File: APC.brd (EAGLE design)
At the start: 24.9 x 56.8 mm, 12 parts, among them IC1 NE556D, J1 POWER_JACKPTH_SMD_COMBO, J3 AUDIO_JACK_3.5MM_PTH, P1 1M, P2 1M, P3 100k

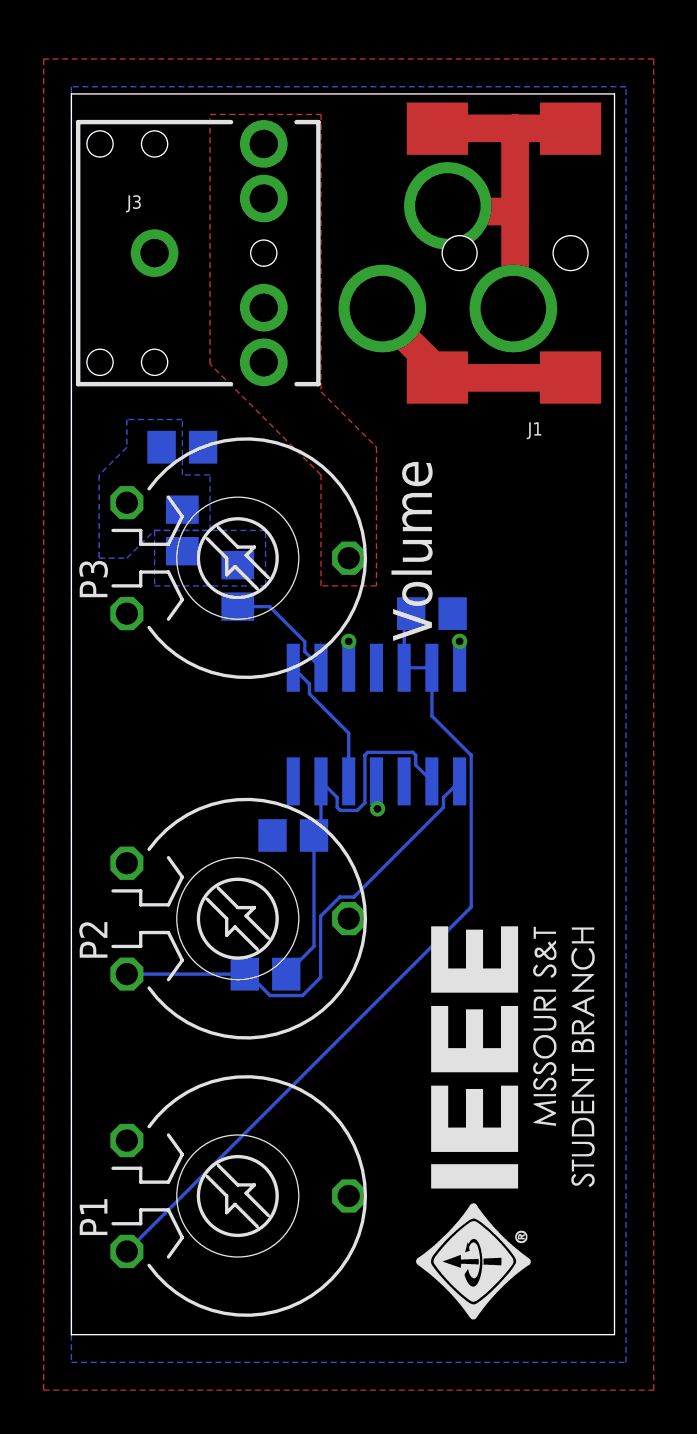
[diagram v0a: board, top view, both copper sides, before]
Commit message: V2
Updated schematic to use all digikey parts. Added solderable pads for power
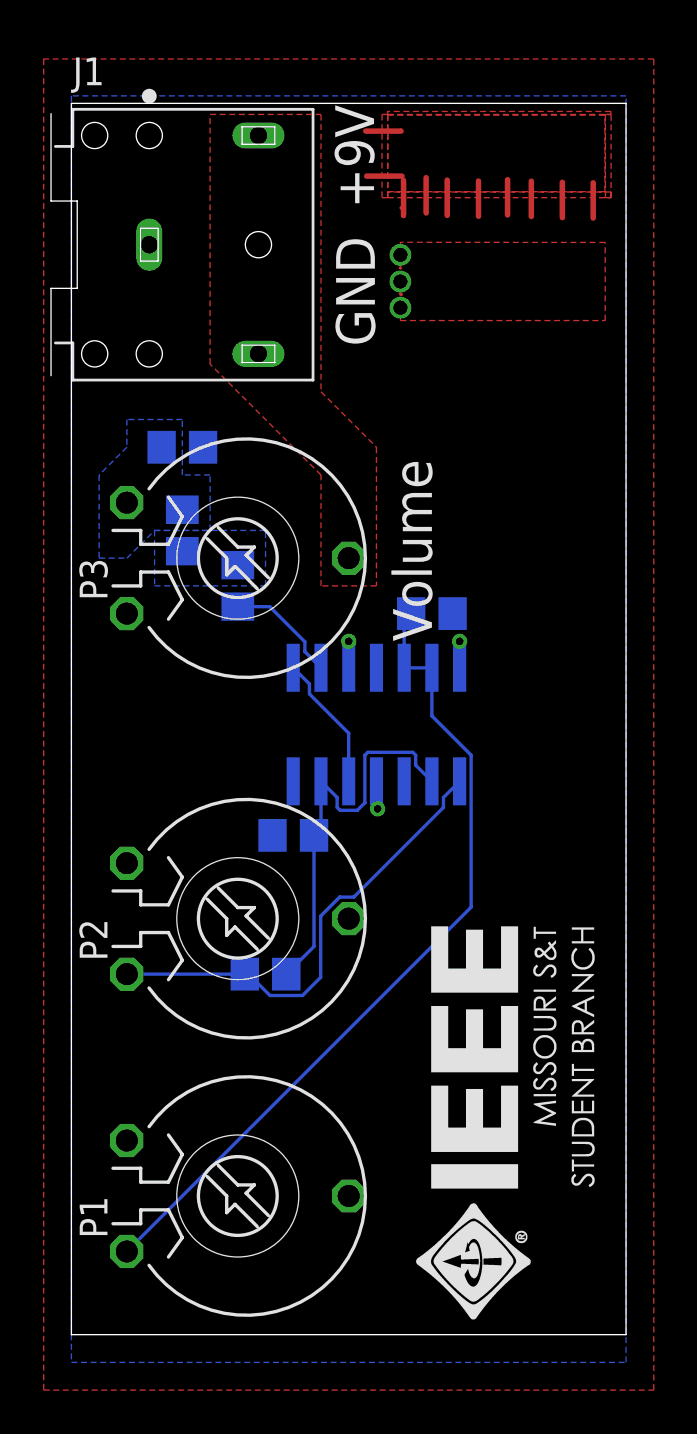
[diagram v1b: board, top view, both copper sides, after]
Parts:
- removed J3: AUDIO_JACK_3.5MM_PTH, SparkFun-Connectors:AUDIO-JACK
- J1: value POWER_JACKPTH_SMD_COMBO -> SJ1-3523N; device SparkFun-Connectors:POWER_JACK_COMBO -> SJ1-3523N:CUI_SJ1-3523N
- moved J1 19.3 mm to (3.57, 93.1), turned to 0 degrees
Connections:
- net +9V: no longer J1.POWER
- net GND: now also J1.1; no longer J1.GND, J1.GND@1, J3.SLEEVE
- net N$9: now also J1.2, J1.3; no longer J3.RING, J3.TIP
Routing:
- net +9V: track 3.70 -> 20.0 mm
- net N$9: track 0.63 -> 0.00 mm
- net GND: track 0.00 -> 0.06 mm, vias 0 -> 3
- added copper zone on layer 1, net GND
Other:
- board size 24.9 x 56.8 mm -> 25.4 x 56.4 mm
- board text added: "+9V"
- board text added: "GND"

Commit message: JLC Gerber created
Ready for ordering
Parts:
- renumbered R4 to R2, R6 to R3
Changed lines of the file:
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@@
 <attribute name="SPICEPREFIX" value="C" x="7.62" y="77.47" size="1.778" layer="28" rot="MR90" display="off"/>
 </element>
-<element name="R4" library="rcl" library_urn="urn:adsk.eagle:library:334" package="R0805" package3d_urn="urn:adsk.eagle:package:23553/2" value="10k" x="5.08" y="80.01" smashed="yes" rot="MR90">
+<element name="R2" library="rcl" library_urn="urn:adsk.eagle:library:334" package="R0805" package3d_urn="urn:adsk.eagle:package:23553/2" value="10k" x="5.08" y="80.01" smashed="yes" rot="MR90">
 <attribute name="NAME" x="6.35" y="79.375" size="1.27" layer="26" rot="MR90"/>
 <attribute name="POPULARITY" value="85" x="5.08" y="80.01" size="1.778" layer="28" rot="MR90" display="off"/>
@@
 <attribute name="POPULARITY" value="0" x="7.62" y="78.74" size="1.778" layer="27" rot="R270" display="off"/>
 </element>
-<element name="R6" library="rcl" library_urn="urn:adsk.eagle:library:334" package="R0805" package3d_urn="urn:adsk.eagle:package:23553/2" value="4.7k" x="5.08" y="83.82" smashed="yes" rot="MR0">
+<element name="R3" library="rcl" library_urn="urn:adsk.eagle:library:334" package="R0805" package3d_urn="urn:adsk.eagle:package:23553/2" value="4.7k" x="5.08" y="83.82" smashed="yes" rot="MR0">
 <attribute name="NAME" x="5.715" y="85.09" size="1.27" layer="26" rot="MR0"/>
 <attribute name="POPULARITY" value="85" x="5.08" y="83.82" size="1.778" layer="28" rot="MR0" display="off"/>
@@
 <contactref element="C2" pad="2"/>
 <contactref element="P3" pad="E"/>
-<contactref element="R6" pad="1"/>
+<contactref element="R3" pad="1"/>
 <polygon width="0.1524" layer="16" rank="6">
 <vertex x="0" y="99.9134375"/>
@@
 <signal name="N$5">
 <contactref element="C3" pad="2"/>
-<contactref element="R4" pad="1"/>
+<contactref element="R2" pad="1"/>
 <polygon width="0.1524" layer="16" rank="2">
 <vertex x="3.81" y="80.01"/>
@@
 </signal>
 <signal name="N$10">
-<contactref element="R4" pad="2"/>
+<contactref element="R2" pad="2"/>
 <contactref element="P3" pad="A"/>
-<contactref element="R6" pad="2"/>
+<contactref element="R3" pad="2"/>
 <polygon width="0.1524" layer="16">
 <vertex x="2.54" y="83.82"/>
